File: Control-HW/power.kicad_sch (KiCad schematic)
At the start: 12 parts

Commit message: First revision
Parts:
- gave numbers to parts that had none: 12
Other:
- note added: "Running the LDO from 12V lets you use a 1S battery."
- note removed: "Running the step down from 12V lets you use a 1S battery."
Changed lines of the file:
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@@
     (stroke (width 0) (type default) (color 0 0 0 0))
   )
-  (text "Running the step down from 12V lets you use a 1S battery."
-    (at 96.52 114.3 0)
+  (text "Running the LDO from 12V lets you use a 1S battery."
+    (at 85.09 107.95 0)
     (effects (font (size 1.27 1.27)) (justify left bottom))
   )
@@
   (symbol (lib_id "U_Power:AP3015KTR-G1") (at 168.275 53.34 0) (unit 1)
     (in_bom yes) (on_board yes) (fields_autoplaced)
-    (property "Reference" "U?" (id 0) (at 168.275 45.881 0))
+    (property "Reference" "U6" (id 0) (at 168.275 45.881 0))
     (property "Value" "AP3015KTR-G1" (id 1) (at 168.275 48.4179 0))
     (property "Footprint" "U_IC:SOT23_5" (id 2) (at 169.545 71.12 0)
@@
   (symbol (lib_id "U_Power:MCP1755T-3302E{slash}OT") (at 167.64 93.98 0) (unit 1)
     (in_bom yes) (on_board yes) (fields_autoplaced)
-    (property "Reference" "U?" (id 0) (at 167.64 83.4608 0))
+    (property "Reference" "U5" (id 0) (at 167.64 83.4608 0))
     (property "Value" "MCP1755T-3302E/OT" (id 1) (at 167.64 85.9977 0))
     (property "Footprint" "U_IC:SOT23_5" (id 2) (at 176.53 100.33 0)
@@
   (symbol (lib_id "power:+5V") (at 194.31 90.17 0) (unit 1)
     (in_bom yes) (on_board yes)
-    (property "Reference" "#PWR?" (id 0) (at 194.31 93.98 0)
+    (property "Reference" "#PWR034" (id 0) (at 194.31 93.98 0)
       (effects (font (size 1.27 1.27)) hide)
     )
@@
   (symbol (lib_id "C_Capacitor:C_0805") (at 206.375 54.61 0) (unit 1)
     (in_bom yes) (on_board yes) (fields_autoplaced)
-    (property "Reference" "C?" (id 0) (at 208.6991 52.867 0)
+    (property "Reference" "C20" (id 0) (at 208.6991 52.867 0)
       (effects (font (size 1.27 1.27)) (justify left))
     )
@@
   (symbol (lib_id "C_Capacitor:C_0805") (at 194.31 99.06 0) (mirror x) (unit 1)
     (in_bom yes) (on_board yes)
-    (property "Reference" "C?" (id 0) (at 200.66 97.1581 0)
+    (property "Reference" "C19" (id 0) (at 200.66 97.1581 0)
       (effects (font (size 1.27 1.27)) (justify right))
     )
@@
   (symbol (lib_id "R_Resistor:R_0603") (at 192.405 60.96 0) (unit 1)
     (in_bom yes) (on_board yes) (fields_autoplaced)
-    (property "Reference" "R?" (id 0) (at 194.056 59.2107 0)
+    (property "Reference" "R15" (id 0) (at 194.056 59.2107 0)
       (effects (font (size 1.27 1.27)) (justify left))
     )
@@
   (symbol (lib_id "C_Capacitor:C_0805") (at 148.59 99.06 0) (mirror x) (unit 1)
     (in_bom yes) (on_board yes)
-    (property "Reference" "C?" (id 0) (at 146.266 97.3043 0)
+    (property "Reference" "C17" (id 0) (at 146.266 97.3043 0)
       (effects (font (size 1.27 1.27)) (justify right))
     )
@@
   (symbol (lib_id "power:GND") (at 167.64 109.22 0) (unit 1)
     (in_bom yes) (on_board yes) (fields_autoplaced)
-    (property "Reference" "#PWR?" (id 0) (at 167.64 115.57 0)
+    (property "Reference" "#PWR032" (id 0) (at 167.64 115.57 0)
       (effects (font (size 1.27 1.27)) hide)
     )
@@
   (symbol (lib_id "C_Capacitor:C_0805") (at 185.42 99.06 0) (mirror x) (unit 1)
     (in_bom yes) (on_board yes)
-    (property "Reference" "C?" (id 0) (at 191.135 97.1581 0)
+    (property "Reference" "C18" (id 0) (at 191.135 97.1581 0)
       (effects (font (size 1.27 1.27)) (justify right))
     )
@@
   (symbol (lib_id "power:+12V") (at 206.375 36.83 0) (unit 1)
     (in_bom yes) (on_board yes) (fields_autoplaced)
-    (property "Reference" "#PWR?" (id 0) (at 206.375 40.64 0)
+    (property "Reference" "#PWR035" (id 0) (at 206.375 40.64 0)
       (effects (font (size 1.27 1.27)) hide)
     )
@@
   (symbol (lib_id "C_Capacitor:C_0805") (at 147.955 57.15 0) (mirror x) (unit 1)
     (in_bom yes) (on_board yes) (fields_autoplaced)
-    (property "Reference" "C?" (id 0) (at 145.631 55.3943 0)
+    (property "Reference" "C16" (id 0) (at 145.631 55.3943 0)
       (effects (font (size 1.27 1.27)) (justify right))
     )
@@
   (symbol (lib_id "power:GND") (at 168.275 71.12 0) (unit 1)
     (in_bom yes) (on_board yes) (fields_autoplaced)
-    (property "Reference" "#PWR?" (id 0) (at 168.275 77.47 0)
+    (property "Reference" "#PWR033" (id 0) (at 168.275 77.47 0)
       (effects (font (size 1.27 1.27)) hide)
     )
@@
   (symbol (lib_id "L_Inductor:NLCV32T-4R7M-PFR") (at 167.005 39.37 90) (unit 1)
     (in_bom yes) (on_board yes) (fields_autoplaced)
-    (property "Reference" "L?" (id 0) (at 167.005 35.2892 90))
+    (property "Reference" "L1" (id 0) (at 167.005 35.2892 90))
     (property "Value" "NLCV32T-4R7M-PFR" (id 1) (at 167.005 37.8261 90))
     (property "Footprint" "L_Inductor:L_1210" (id 2) (at 169.545 29.21 0)
@@
   (symbol (lib_id "R_Resistor:R_0603") (at 192.405 48.26 0) (unit 1)
     (in_bom yes) (on_board yes) (fields_autoplaced)
-    (property "Reference" "R?" (id 0) (at 194.056 46.5107 0)
+    (property "Reference" "R14" (id 0) (at 194.056 46.5107 0)
       (effects (font (size 1.27 1.27)) (justify left))
     )
@@
   (symbol (lib_id "Jumper:SolderJumper_3_Open") (at 130.175 91.44 90) (unit 1)
     (in_bom no) (on_board yes)
-    (property "Reference" "JP?" (id 0) (at 125.73 91.44 90))
+    (property "Reference" "JP1" (id 0) (at 125.73 91.44 90))
     (property "Value" "~" (id 1) (at 117.475 92.075 90))
     (property "Footprint" "Jumper:SolderJumper-3_P1.3mm_Open_RoundedPad1.0x1.5mm_NumberLabels" (id 2) (at 130.175 91.44 0)
@@
   (symbol (lib_id "D_Diode:DSS110U") (at 186.055 39.37 180) (unit 1)
     (in_bom yes) (on_board yes) (fields_autoplaced)
-    (property "Reference" "D?" (id 0) (at 186.3725 33.7122 0))
+    (property "Reference" "D1" (id 0) (at 186.3725 33.7122 0))
     (property "Value" "DSS110U" (id 1) (at 186.3725 35.6785 0)
       (effects (font (size 0.635 0.635)))
@@
   (symbol (lib_id "power:+12V") (at 125.73 100.33 90) (unit 1)
     (in_bom yes) (on_board yes)
-    (property "Reference" "#PWR?" (id 0) (at 129.54 100.33 0)
-      (effects (font (size 1.27 1.27)) hide)
-    )
+    (property "Reference" "#PWR031" (id 0) (at 129.54 100.33 0)
+      (effects (font (size 1.27 1.27)) hide)
+    )

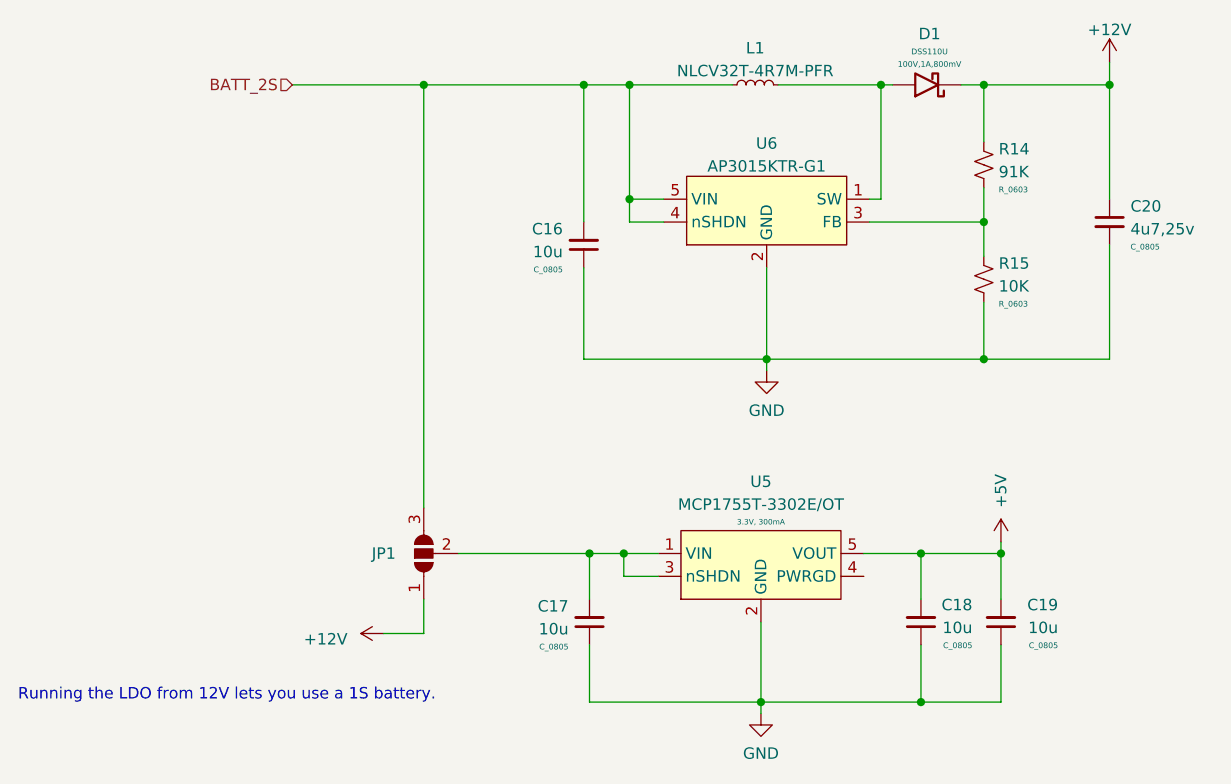
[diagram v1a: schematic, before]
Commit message: Implemented control pcb
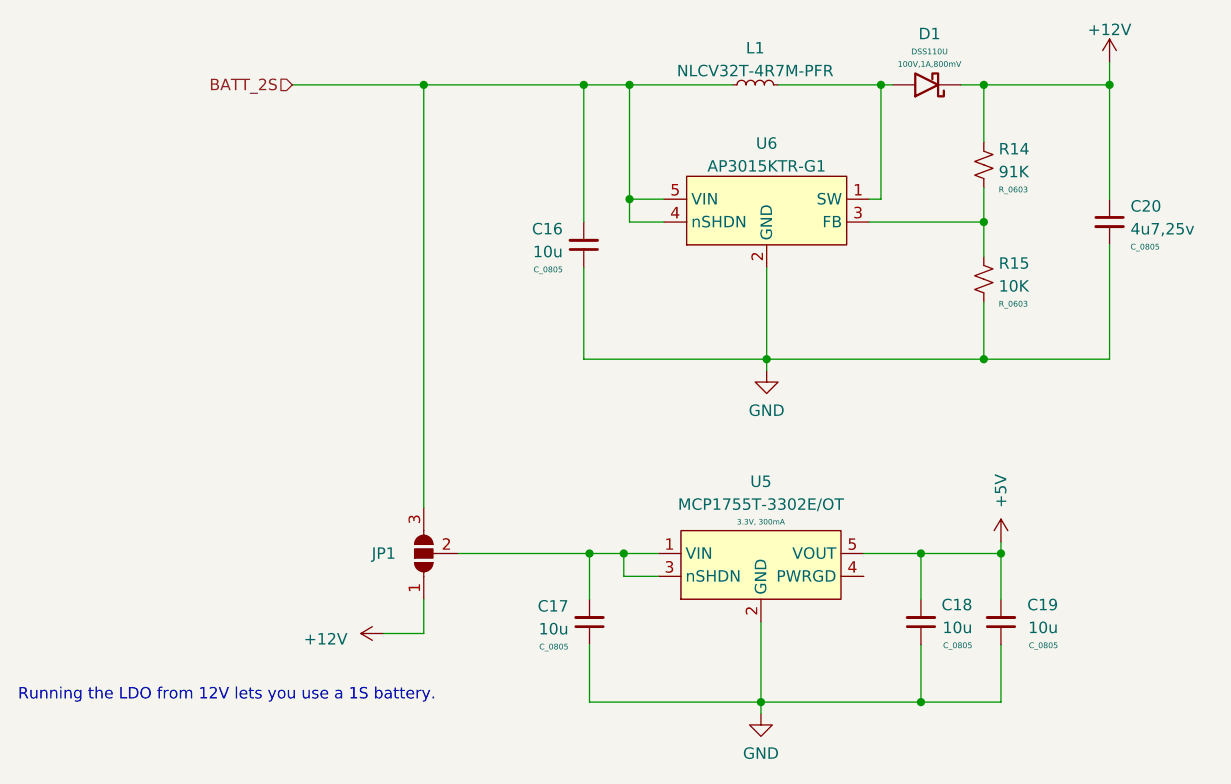
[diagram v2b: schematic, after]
